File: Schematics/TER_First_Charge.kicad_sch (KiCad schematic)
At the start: 2 parts

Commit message: work on schematic, 6/4/2023
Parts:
- added 12V_1, 12V_2: Battery, symbol Device:Battery
- added Break_Over_Travel: Normally Closed, symbol Switch:SW_SPST
- added GLVMS: Hella Disconnect switch, symbol Switch:SW_SPST
- added GLV_Main_Fuse: Fuse, symbol Device:Fuse
- added Left_Side_Switch, Right_Side_Switch: Button Switch, symbol Switch:SW_Push_Open
- added Mainline_Contactor, N_AIR1, P_AIR: 280V Max, Relay_THT:Relay_1P1T_NO_10x24x18.8mm_Panasonic_ADW11xxxxW_THT, symbol Relay:ADW11
- added Precharge_Contactor: SPDT, Relay_THT:Relay_SPDT_Finder_36.11, symbol Relay:FINDER-36.11
- added Precharge_Res: 750, symbol Device:R
- added TractionFuse: 125A, symbol Device:Fuse
- added U1: ~, symbol TER:SevconG4S8
- Box1: renamed from BT1; value Battery -> 140V
- Box2: renamed from BT2; value Battery -> 140V
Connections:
- net Virtual Accumulator: now reaches Box1.2 (-), Box2.1 (+)
- net at Box2.2 (-): now also N_AIR1.5
- net at Box1.1 (+): now also P_AIR.5
- new net: Mainline_Contactor.3, Precharge_Res.1, U1.36 (B+)
- new net: Mainline_Contactor.5, TractionFuse.2
- new net: P_AIR.3, Precharge_Contactor.14, TractionFuse.1
- new net: 12V_1.1 (+), GLV_Main_Fuse.2
- new net: 12V_1.2 (-), 12V_2.1 (+)
- new net: Break_Over_Travel.1 (A), Left_Side_Switch.2 (B)
- new net: N_AIR1.3, Precharge_Contactor.12, U1.37 (B-)
- new net: GLVMS.1 (A), GLV_Main_Fuse.1
- new net: GLVMS.2 (B), Right_Side_Switch.1 (A)
- new net: Left_Side_Switch.1 (A), Right_Side_Switch.2 (B)
- new net: Precharge_Contactor.11, Precharge_Res.2
- new net AIR_High0: N_AIR1.6
- new net AIR_High1: P_AIR.6
- new net AIR_LOW1: P_AIR.1
- new net AIR_Low0: N_AIR1.1
- new net GND: 12V_2.2 (-)
- no-connect marks 0 -> 1
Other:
- note added: "120A (Assuming Max discharge) In Conduit"
- note added: "500V - FWH-125B Bussmann"
- note added: "Connect Ground to Chassis"
- note added: "If possible, put this before the AIR inside the box"
- note added: "LFX36L3-BS12 Shorai 12V, 12Ah Max dischagre 24A"
- note added: "OHMITE 50W 1351"
- note added: "OMRON A22-1 NC"
- note added: "Precharge circuit must not be fused"
- note added: "determine min rating for fuse"
- company: (none) -> Tufts Electric Racing
- title: (none) -> First Charge Overview
- moved on the sheet: Box1, Box2

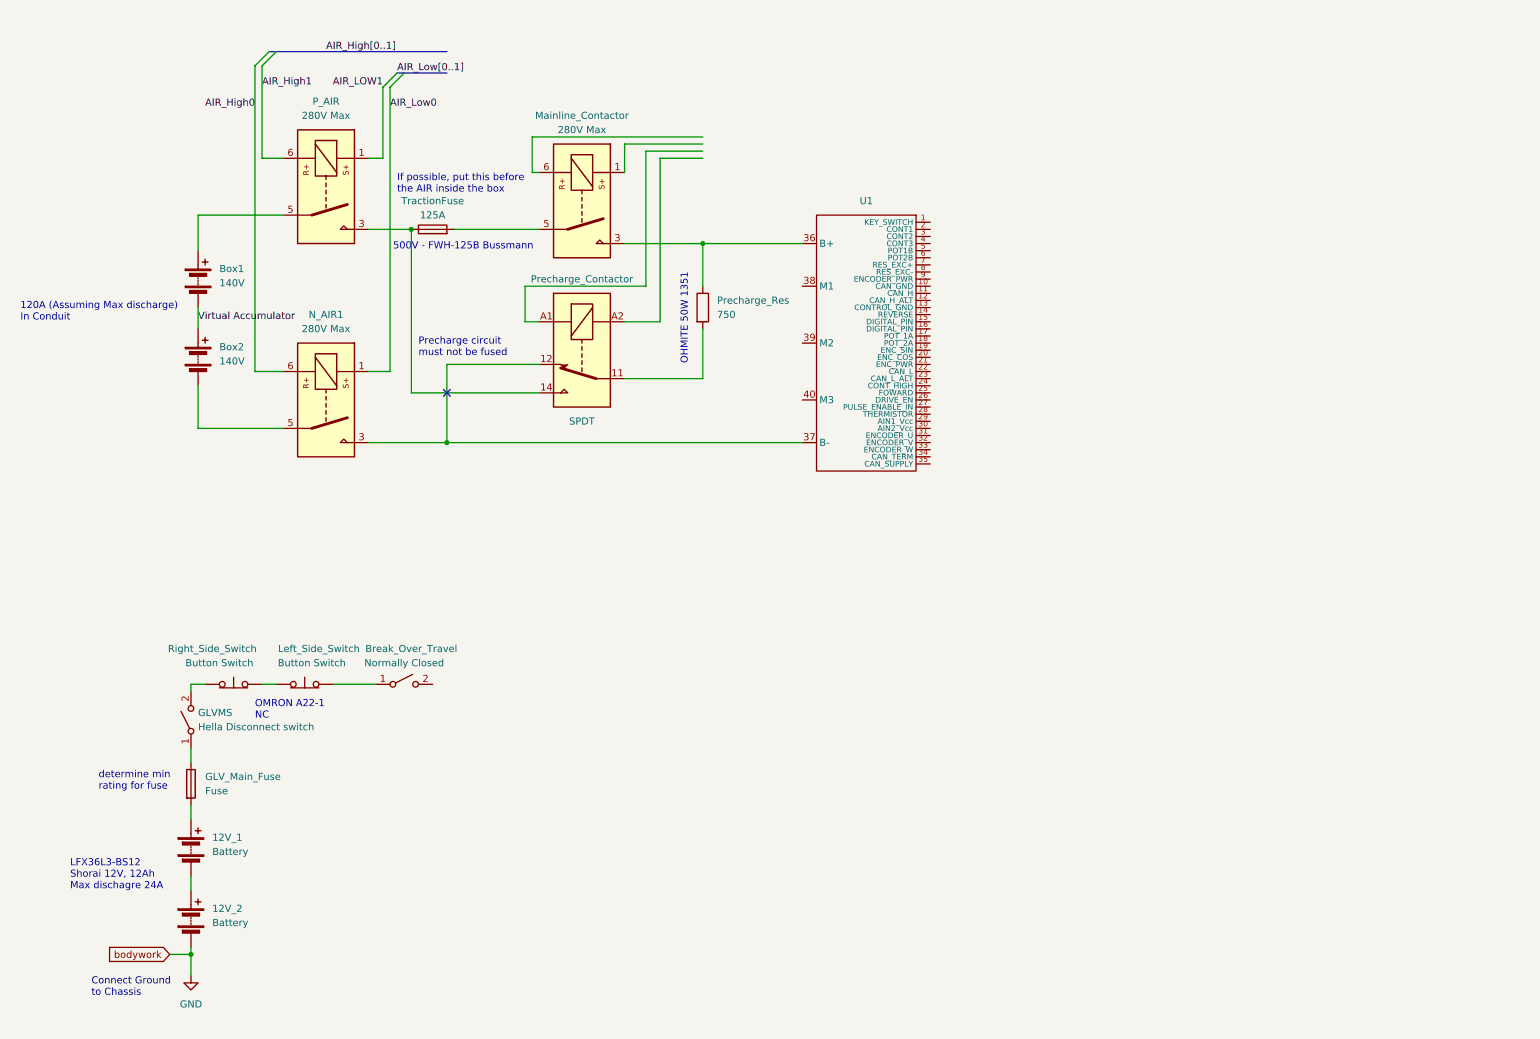
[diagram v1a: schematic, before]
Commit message: 6/6/2023, IMD symbol needed
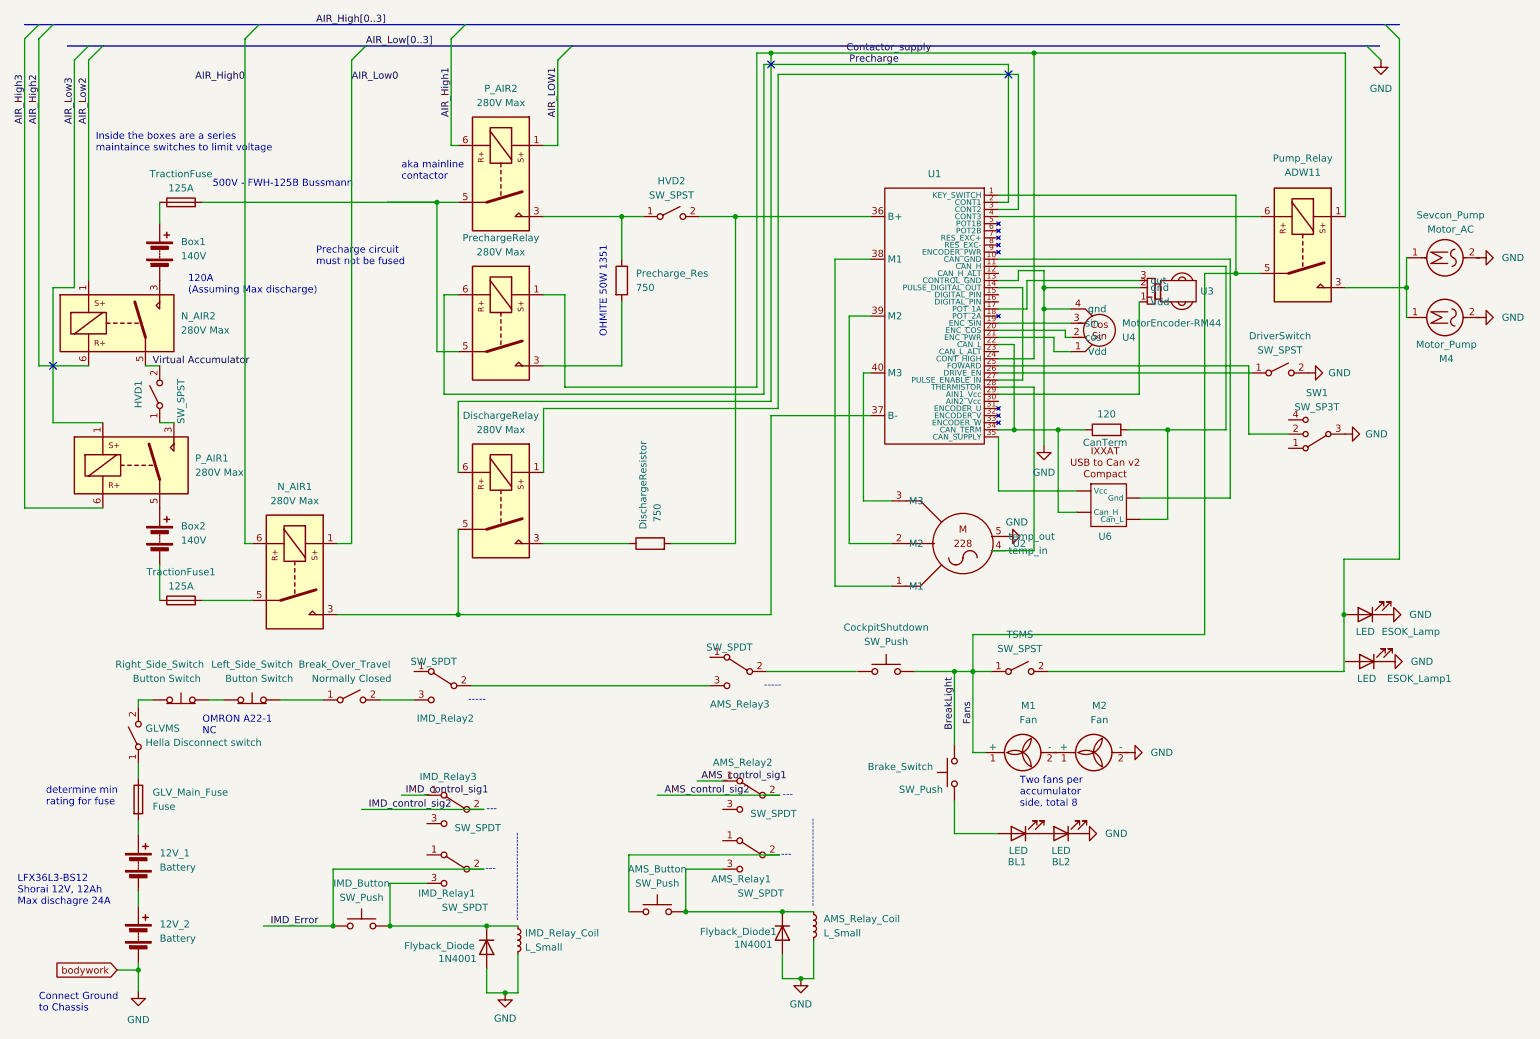
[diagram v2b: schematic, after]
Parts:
- removed P_AIR: 280V Max, Relay_THT:Relay_1P1T_NO_10x24x18.8mm_Panasonic_ADW11xxxxW_THT, symbol Relay:ADW11
- removed Precharge_Contactor: SPDT, Relay_THT:Relay_SPDT_Finder_36.11, symbol Relay:FINDER-36.11
- added AMS_Button, Brake_Switch, CockpitShutdown, IMD_Button: SW_Push, symbol Switch:SW_Push
- added AMS_Relay1, AMS_Relay2, AMS_Relay3, IMD_Relay1, IMD_Relay2, IMD_Relay3: SW_SPDT, symbol Switch:SW_SPDT
- added AMS_Relay_Coil, IMD_Relay_Coil: L_Small, symbol Device:L_Small
- added BL1, BL2, ESOK_Lamp, ESOK_Lamp1: LED, symbol Device:LED
- added CanTerm: 120, symbol Device:R
- added DischargeRelay, N_AIR2, P_AIR1, PrechargeRelay: 280V Max, Relay_THT:Relay_1P1T_NO_10x24x18.8mm_Panasonic_ADW11xxxxW_THT, symbol Relay:ADW11
- added DischargeResistor: 750, symbol Device:R
- added DriverSwitch, HVD1, HVD2, TSMS: SW_SPST, symbol Switch:SW_SPST
- added Flyback_Diode, Flyback_Diode1: 1N4001, Diode_THT:D_DO-41_SOD81_P10.16mm_Horizontal, symbol Diode:1N4001
- added M1, M2: Fan, symbol Motor:Fan
- added M4: Motor_Pump, symbol Motor:Motor_AC
- added Pump_Relay: ADW11, Relay_THT:Relay_1P1T_NO_10x24x18.8mm_Panasonic_ADW11xxxxW_THT, symbol Relay:ADW11
- added SW1: SW_SP3T, symbol Switch:SW_SP3T
- added Sevcon_Pump: Motor_AC, symbol Motor:Motor_AC
- added TractionFuse1: 125A, symbol Device:Fuse
- added U2: ~, symbol TER:Emrax_228
- added U3: ~, symbol TER:Hall_Effect_Sensor
- added U4: MotorEncoder-RM44, symbol TER:MotorEncoder-RM44
- added U6: ~, symbol TER:IXXAT_Canbus
- renumbered Mainline_Contactor to P_AIR2
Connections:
- net AIR_High1: now also P_AIR2.6
- net AIR_LOW1: now also P_AIR2.1
- net GND: now also U1.13 (CONTROL_GND), AMS_Relay_Coil.2, BL2.1 (K), DriverSwitch.2 (B), ESOK_Lamp.1 (K), ESOK_Lamp1.1 (K), Flyback_Diode.2 (A), Flyback_Diode1.2 (A), IMD_Relay_Coil.2, M2.2 (-), M4.2, SW1.3, Sevcon_Pump.2, U3.2 (gnd), U4.4 (gnd)
- net Virtual Accumulator: now also HVD1.2 (B), N_AIR2.5; no longer Box1.2 (-), Box2.1 (+)
- net at P_AIR2.3, Precharge_Res.1: now also HVD2.1 (A); no longer U1.36 (B+)
- net at P_AIR2.5, TractionFuse.2: now also PrechargeRelay.5
- net at TractionFuse.1: now also Box1.1 (+)
- net at Box2.2 (-): now also TractionFuse1.1; no longer N_AIR1.5
- net at Break_Over_Travel.2 (B): now also IMD_Relay2.3 (C)
- net at N_AIR1.3, U1.37 (B-): now also DischargeRelay.5
- net BreakLight: now reaches U1.1 (KEY_SWITCH)
- net BreakLight: now also Brake_Switch.2, CockpitShutdown.2, M1.1 (+), Pump_Relay.5, TSMS.1 (A)
- net at U1.10 (CAN_GND): now also U6. (Vcc)
- net at U1.11 (CAN_H): now also CanTerm.2, U6. (Vcc)
- net at U1.14 (PULSE_DIGITAL_OUT): now also U1.27 (PULSE_ENABLE_IN)
- net at U1.17 (POT_1A): now also U3.3 (out)
- net at U1.19 (ENC_SIN): now also U4.3 (sin)
- net Precharge: now reaches U1.2 (CONT1)
- net Precharge: now also PrechargeRelay.6
- net at U1.20 (ENC_COS): now also U4.2 (cos)
- net at U1.21 (ENC_PWR): now also U4.1 (Vdd)
- net at U1.22 (CAN_L): now also U1.34 (CAN_TERM), CanTerm.1, U6. (Vcc)
- net Contactor_supply: now reaches U1.24 (CONT_HIGH)
- net Contactor_supply: now also DischargeRelay.6, PrechargeRelay.1, Pump_Relay.1
- net at U1.25 (FOWARD): now also SW1.2
- net at U1.26 (DRIVE_EN): now also DriverSwitch.1 (A)
- net at U1.28 (THERMISTOR): now also U2.4 (temp_in)
- net at U1.29 (AIN1_Vcc): now also U3.1 (Vdd)
- net at U1.3 (CONT2): now also DischargeRelay.1
- net at U1.35 (CAN_SUPPLY): now also U6. (Vcc)
- net at U1.38 (M1): now also U2.1 (M1)
- net at U1.39 (M2): now also U2.2 (M2)
- net at U1.4 (CONT3): now also Pump_Relay.6
- net at U1.40 (M3): now also U2.3 (M3)
- net at Precharge_Res.2: now also PrechargeRelay.3
- new net: AMS_Button.1, AMS_Relay1.2 (B)
- new net: AMS_Button.2, AMS_Relay1.3 (C), AMS_Relay_Coil.1, Flyback_Diode1.1 (K)
- new net: Box2.1 (+), P_AIR1.5
- new net: M4.1, Pump_Relay.3, Sevcon_Pump.1
- new net: AMS_Relay3.3 (C), IMD_Relay2.2 (B)
- new net: Flyback_Diode.1 (K), IMD_Button.2, IMD_Relay1.3 (C), IMD_Relay_Coil.1
- new net: ESOK_Lamp.2 (A), TSMS.2 (B)
- new net: N_AIR1.5, TractionFuse1.2
- new net: HVD1.1 (A), P_AIR1.3
- new net: M1.2 (-), M2.1 (+)
- new net: DischargeRelay.3, DischargeResistor.1
- new net: DischargeResistor.2, HVD2.2 (B), U1.36 (B+)
- new net: BL1.1 (K), BL2.2 (A)
- new net: BL1.2 (A), Brake_Switch.1
- new net: Box1.2 (-), N_AIR2.3
- new net AIR_High2: N_AIR2.6
- new net AIR_High3: P_AIR1.6
- new net AIR_Low2: N_AIR2.1
- new net AIR_Low3: P_AIR1.1
- new net AMS_control_sig1: AMS_Relay2.1 (A)
- new net AMS_control_sig2: AMS_Relay2.2 (B)
- new net IMD_Error: IMD_Button.1, IMD_Relay1.2 (B)
- new net IMD_control_sig1: IMD_Relay3.1 (A)
- new net IMD_control_sig2: IMD_Relay3.2 (B)
- no-connect marks 1 -> 3
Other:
- note added: "---"
- note added: "-----"
- note added: "-------------------------"
- note added: "120A (Assuming Max discharge)"
- note added: "Inside the boxes are a series maintaince switches to limit voltage"
- note added: "Two fans per accumulator side, total 8"
- note added: "aka mainline contactor"
- note removed: "120A (Assuming Max discharge) In Conduit"
- note removed: "If possible, put this before the AIR inside the box"
- moved on the sheet: 12V_1, 12V_2, Box1, Box2, Break_Over_Travel, GLVMS, GLV_Main_Fuse, Left_Side_Switch, N_AIR1, P_AIR2, Precharge_Res, Right_Side_Switch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

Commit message: 6/7/2023, IMD Added
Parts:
- added DC_Converter: 24V-12V, Converter_DCDC:Converter_DCDC_XP_POWER-IAxxxxS_THT, symbol Converter_DCDC:IA0503S
- added U5: ~, symbol TER:IMD
- renumbered SW1 to Forward_Reverse
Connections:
- net GND: now also DC_Converter.2 (-Vin), DC_Converter.4 (-Vout), DC_Converter.5 (0V), U5.1.1 (Chassis_1), U5.1.7 (Chassis_2)
- net IMD_Error: now also U5.1.3 (Error)
- net at Forward_Reverse.4: now also U1.15 (DIGITAL_PIN)
- net at ESOK_Lamp.2 (A), TSMS.2 (B): now also DC_Converter.1 (+Vin)
- net at DischargeRelay.5, N_AIR1.3, U1.37 (B-): now also U5.2.8 (HV1_N)
- net at DischargeResistor.2, HVD2.2 (B), U1.36 (B+): now also U5.2.1 (HV1_P)
- new net: DC_Converter.6 (+Vout), U5.1.8 (Vcc_12V)
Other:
- moved on the sheet: AMS_Button, AMS_Relay1, AMS_Relay2, AMS_Relay3, AMS_Relay_Coil, BL1, BL2, Brake_Switch, CockpitShutdown, ESOK_Lamp, ESOK_Lamp1, Flyback_Diode1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
